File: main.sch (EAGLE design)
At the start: 117 parts, among them Q1 2N2222, Q2 2N2222, Q3 2N2222, Q4 N_MOSFET_DEVSOT23-6L_PKG, U1 MAX_485_DEV3D, U2 BQ24072TRGTR_DEVBQ24072TRGTR, U3 LD1117S33CTR_DEVLD1117S33CTR, U4 ESP_32_WROVER_I_PKG, U5 USB_TO_UART_DEV, U6 AP9214L_DEV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

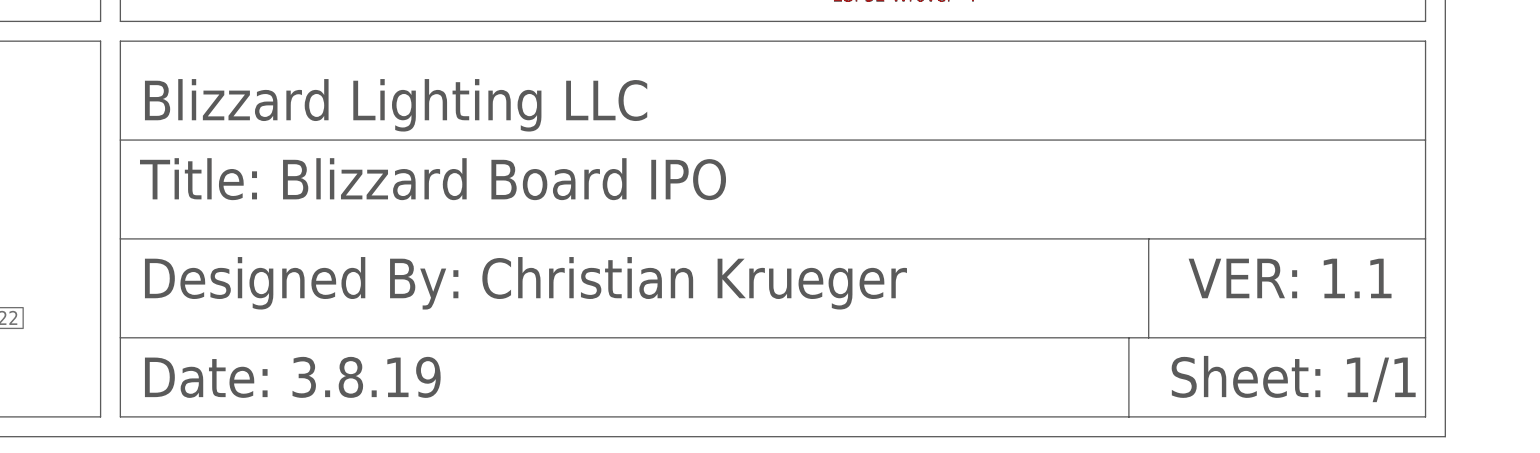
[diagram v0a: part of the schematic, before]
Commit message: fixed tab problems plus made some simplifications
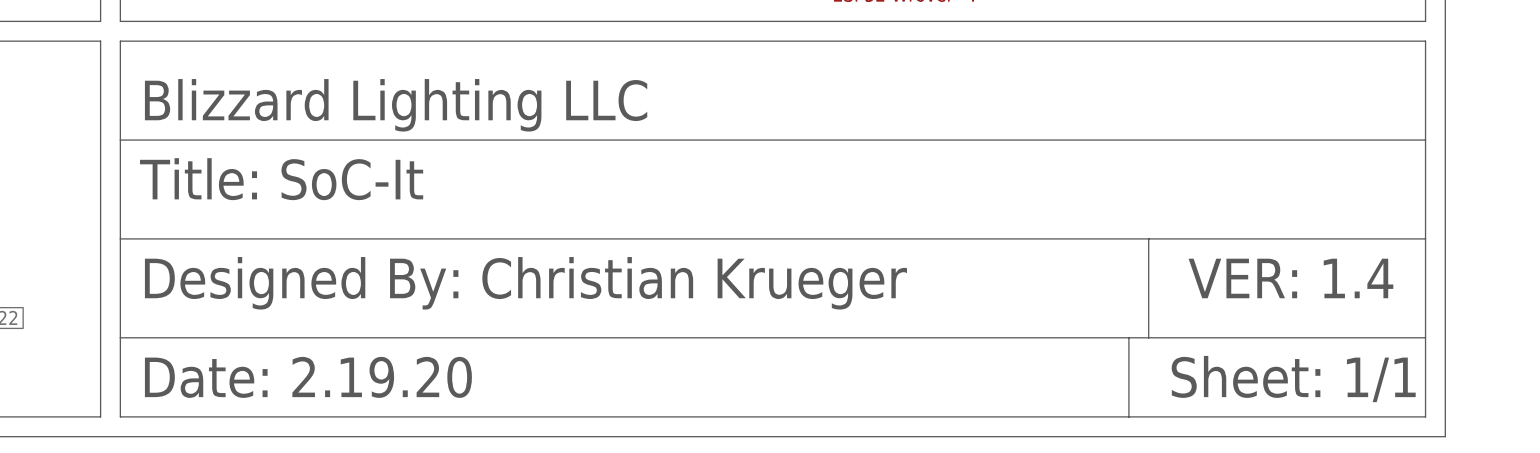
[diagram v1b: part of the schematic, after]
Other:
- note added: "Date: 2.19.20"
- note added: "Title: SoC-It"
- note added: "VER: 1.4"
- note removed: "Date: 3.8.19"
- note removed: "Title: Blizzard Board IPO"
- note removed: "VER: 1.1"
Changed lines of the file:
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@@
 <parts>
 <part name="U1" library="Blizzard_Library" library_urn="urn:adsk.eagle:library:2665040" deviceset="MAX_485_DEV" device="3D" package3d_urn="urn:adsk.eagle:package:2665057/5"/>
-<part name="X1" library="Blizzard_Library" library_urn="urn:adsk.eagle:library:2665040" deviceset="XLR_FEMALE_PLUG_DEV" device="" package3d_urn="urn:adsk.eagle:package:2725172/9"/>
+<part name="X1" library="Blizzard_Library" library_urn="urn:adsk.eagle:library:2665040" deviceset="XLR_FEMALE_PLUG_DEV" device="" package3d_urn="urn:adsk.eagle:package:2725172/12"/>
 <part name="Q1" library="Blizzard_Library" library_urn="urn:adsk.eagle:library:2665040" deviceset="SOT23_TRANS" device="3D" package3d_urn="urn:adsk.eagle:package:2669417/4" value="2N2222"/>
 <part name="Q2" library="Blizzard_Library" library_urn="urn:adsk.eagle:library:2665040" deviceset="SOT23_TRANS" device="3D" package3d_urn="urn:adsk.eagle:package:2669417/4" value="2N2222"/>
@@
 <wire x1="226.06" y1="-302.26" x2="261.62" y2="-302.26" width="0.1524" layer="97"/>
 <wire x1="93.98" y1="-314.96" x2="223.52" y2="-314.96" width="0.1524" layer="97"/>
-<text x="96.52" y="-297.18" size="5.08" layer="97">Title: Blizzard Board IPO</text>
+<text x="96.52" y="-297.18" size="5.08" layer="97">Title: SoC-It</text>
 <text x="96.52" y="-309.88" size="5.08" layer="97">Designed By: Christian Krueger</text>
 <text x="96.52" y="-287.02" size="5.08" layer="97">Blizzard Lighting LLC</text>
-<text x="96.52" y="-322.58" size="5.08" layer="97">Date: 3.8.19</text>
+<text x="96.52" y="-322.58" size="5.08" layer="97">Date: 2.19.20</text>
 <text x="228.6" y="-322.58" size="5.08" layer="97">Sheet: 1/1</text>
-<text x="231.14" y="-309.88" size="5.08" layer="97">VER: 1.1</text>
+<text x="231.14" y="-309.88" size="5.08" layer="97">VER: 1.4</text>
 <wire x1="223.52" y1="-314.96" x2="226.06" y2="-314.96" width="0.1524" layer="97"/>
 <wire x1="226.06" y1="-314.96" x2="261.62" y2="-314.96" width="0.1524" layer="97"/>

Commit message: made the aperature size a bit bigger .3 -> .34
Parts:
- removed VCC: VDD USB, Blizzard_Library:VCC
- added NC30, NC31, NC32, NC33, NC34, NC35, NC36, NC37, NC38, NC39, NC40: NC, Blizzard_Library:NC
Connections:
- new net N$41: NC30.P$1, U5.NC0
- new net N$42: NC31.P$1, U5.NC2
- new net N$43: NC32.P$1, U5.NC1
- new net N$44: NC33.P$1, U5.NC3
- new net N$45: NC34.P$1, U5.NC4
- new net N$46: NC35.P$1, U5.NC5
- new net N$47: NC36.P$1, U5.NC6
- new net N$48: NC37.P$1, U5.NC7
- new net N$49: NC38.P$1, U5.NC8
- new net N$50: NC39.P$1, U5.NC9
- new net N$51: NC40.P$1, U5.NC10
- net VDD_USB: no longer U5.NC0, U5.NC1, U5.NC10, U5.NC2, U5.NC3, U5.NC4, U5.NC5, U5.NC6, U5.NC7, U5.NC8, U5.NC9, VCC.P$1

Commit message: v1.5
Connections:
- net 4.2V: no longer U2.OUT2
- net VBAT: no longer U2.BAT2
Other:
- note added: "VER: 1.5"
- note removed: "VER: 1.4"
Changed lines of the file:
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@@
 <part name="C9" library="Blizzard_Library" library_urn="urn:adsk.eagle:library:2665040" deviceset="0603_CAP_DEV" device="3D" package3d_urn="urn:adsk.eagle:package:2669409/4" value="0.1uF"/>
 <part name="U4" library="Blizzard_Library" library_urn="urn:adsk.eagle:library:2665040" deviceset="ESP_32_WROVER_I_PKG" device="" package3d_urn="urn:adsk.eagle:package:4432905/9"/>
-<part name="U5" library="Blizzard_Library" library_urn="urn:adsk.eagle:library:2665040" deviceset="USB_TO_UART_DEV" device="" package3d_urn="urn:adsk.eagle:package:2665053/7"/>
+<part name="U5" library="Blizzard_Library" library_urn="urn:adsk.eagle:library:2665040" deviceset="USB_TO_UART_DEV" device="" package3d_urn="urn:adsk.eagle:package:2665053/9"/>
 <part name="C11" library="Blizzard_Library" library_urn="urn:adsk.eagle:library:2665040" deviceset="0603_CAP_DEV" device="3D" package3d_urn="urn:adsk.eagle:package:2669409/4" value="0.1uF"/>
 <part name="R16" library="Blizzard_Library" library_urn="urn:adsk.eagle:library:2665040" deviceset="0603_RES_DEV" device="3D" package3d_urn="urn:adsk.eagle:package:2685918/4" value="9K"/>
@@
 <part name="GND19" library="Blizzard_Library" library_urn="urn:adsk.eagle:library:2665040" deviceset="GND" device=""/>
 <part name="C14" library="Blizzard_Library" library_urn="urn:adsk.eagle:library:2665040" deviceset="0603_CAP_DEV" device="3D" package3d_urn="urn:adsk.eagle:package:2669409/4" value="0.1uF"/>
-<part name="U2" library="Blizzard_Library" library_urn="urn:adsk.eagle:library:2665040" deviceset="BQ24072TRGTR_DEV" device="BQ24072TRGTR" package3d_urn="urn:adsk.eagle:package:7249956/7"/>
 <part name="GND8" library="Blizzard_Library" library_urn="urn:adsk.eagle:library:2665040" deviceset="GND" device=""/>
 <part name="GND9" library="Blizzard_Library" library_urn="urn:adsk.eagle:library:2665040" deviceset="GND" device=""/>
@@
 <part name="NC39" library="Blizzard_Library" library_urn="urn:adsk.eagle:library:2665040" deviceset="NC" device=""/>
 <part name="NC40" library="Blizzard_Library" library_urn="urn:adsk.eagle:library:2665040" deviceset="NC" device=""/>
+<part name="U2" library="Blizzard_Library" library_urn="urn:adsk.eagle:library:2665040" deviceset="BQ24072TRGTR_DEV" device="BQ24072TRGTR" package3d_urn="urn:adsk.eagle:package:7249956/11"/>
 </parts>
 <sheets>
@@
 <text x="96.52" y="-322.58" size="5.08" layer="97">Date: 2.19.20</text>
 <text x="228.6" y="-322.58" size="5.08" layer="97">Sheet: 1/1</text>
-<text x="231.14" y="-309.88" size="5.08" layer="97">VER: 1.4</text>
+<text x="231.14" y="-309.88" size="5.08" layer="97">VER: 1.5</text>
 <wire x1="223.52" y1="-314.96" x2="226.06" y2="-314.96" width="0.1524" layer="97"/>
 <wire x1="226.06" y1="-314.96" x2="261.62" y2="-314.96" width="0.1524" layer="97"/>
@@
 <attribute name="VALUE" x="21.336" y="-306.07" size="0.8128" layer="94" rot="R90"/>
 </instance>
-<instance part="U2" gate="G$1" x="93.98" y="-119.38" smashed="yes">
-<attribute name="NAME" x="83.82" y="-104.14" size="1.778" layer="94"/>
-</instance>
 <instance part="GND8" gate="G$1" x="93.98" y="-139.7" smashed="yes"/>
 <instance part="GND9" gate="G$1" x="99.06" y="-139.7" smashed="yes"/>
@@
 <instance part="NC39" gate="G$1" x="251.46" y="-73.66" smashed="yes" rot="R270"/>
 <instance part="NC40" gate="G$1" x="238.76" y="-60.96" smashed="yes"/>
+<instance part="U2" gate="G$1" x="93.98" y="-119.38" smashed="yes">
+<attribute name="NAME" x="76.2" y="-104.14" size="1.778" layer="94"/>
+<attribute name="PN" x="104.14" y="-132.08" size="1.27" layer="94"/>
+</instance>
 </instances>
 <busses>
@@
 </segment>
 <segment>
-<pinref part="U2" gate="G$1" pin="EN1"/>
 <pinref part="GND8" gate="G$1" pin="P$1"/>
 <wire x1="93.98" y1="-137.16" x2="93.98" y2="-134.62" width="0.1524" layer="91"/>
+<pinref part="U2" gate="G$1" pin="EN1"/>
 </segment>
 <segment>
-<pinref part="U2" gate="G$1" pin="VSS"/>
 <wire x1="99.06" y1="-134.62" x2="99.06" y2="-137.16" width="0.1524" layer="91"/>
 <pinref part="GND9" gate="G$1" pin="P$1"/>
+<pinref part="U2" gate="G$1" pin="VSS"/>
 </segment>
 <segment>
 <pinref part="C3" gate="G$1" pin="P$1"/>
-<pinref part="U2" gate="G$1" pin="!CE"/>
 <wire x1="71.12" y1="-121.92" x2="78.74" y2="-121.92" width="0.1524" layer="91"/>
 <wire x1="71.12" y1="-121.92" x2="71.12" y2="-124.46" width="0.1524" layer="91"/>
 <junction x="71.12" y="-121.92"/>
 <pinref part="GND5" gate="G$1" pin="P$1"/>
+<pinref part="U2" gate="G$1" pin="!CE"/>
 </segment>
 <segment>
-<pinref part="U2" gate="G$1" pin="TD/OFF"/>
 <wire x1="93.98" y1="-101.6" x2="93.98" y2="-88.9" width="0.1524" layer="91"/>
 <wire x1="93.98" y1="-88.9" x2="96.52" y2="-88.9" width="0.1524" layer="91"/>
@@
 <wire x1="99.06" y1="-88.9" x2="99.06" y2="-93.98" width="0.1524" layer="91"/>
 <pinref part="C4" gate="G$1" pin="P$2"/>
+<pinref part="U2" gate="G$1" pin="TD/OFF"/>
 </segment>
 <segment>
@@
 </segment>
 <segment>
-<pinref part="U2" gate="G$1" pin="BAT2"/>
-<wire x1="78.74" y1="-119.38" x2="76.2" y2="-119.38" width="0.1524" layer="91"/>
-<wire x1="76.2" y1="-119.38" x2="76.2" y2="-116.84" width="0.1524" layer="91"/>
-<pinref part="U2" gate="G$1" pin="BAT1"/>
-<wire x1="76.2" y1="-116.84" x2="78.74" y2="-116.84" width="0.1524" layer="91"/>
 <pinref part="C3" gate="G$1" pin="P$2"/>
-<wire x1="71.12" y1="-116.84" x2="76.2" y2="-116.84" width="0.1524" layer="91"/>
-<junction x="76.2" y="-116.84"/>
+<wire x1="71.12" y1="-116.84" x2="78.74" y2="-116.84" width="0.1524" layer="91"/>
 <wire x1="71.12" y1="-116.84" x2="71.12" y2="-114.3" width="0.1524" layer="91"/>
 <junction x="71.12" y="-116.84"/>
 <pinref part="VCC6" gate="G$1" pin="P$1"/>
+<pinref part="U2" gate="G$1" pin="BAT1"/>
 </segment>
 <segment>
@@
 </segment>
 <segment>
-<pinref part="U2" gate="G$1" pin="IN"/>
 <wire x1="99.06" y1="-101.6" x2="99.06" y2="-99.06" width="0.1524" layer="91"/>
 <pinref part="C4" gate="G$1" pin="P$1"/>
@@
 <junction x="99.06" y="-99.06"/>
 <pinref part="VCC4" gate="G$1" pin="P$1"/>
+<pinref part="U2" gate="G$1" pin="IN"/>
 </segment>
 <segment>
@@
 </segment>
 <segment>
-<pinref part="U2" gate="G$1" pin="!PGOOD"/>
 <wire x1="96.52" y1="-134.62" x2="96.52" y2="-142.24" width="0.1524" layer="91"/>
 <wire x1="96.52" y1="-142.24" x2="124.46" y2="-142.24" width="0.1524" layer="91"/>
@@
 <pinref part="R12" gate="G$1" pin="P$1"/>
 <wire x1="124.46" y1="-134.62" x2="124.46" y2="-142.24" width="0.1524" layer="91"/>
+<pinref part="U2" gate="G$1" pin="!PGOOD"/>
 </segment>
 </net>
@@
 </segment>
 <segment>
-<pinref part="U2" gate="G$1" pin="!CHG"/>
 <wire x1="111.76" y1="-121.92" x2="111.76" y2="-139.7" width="0.1524" layer="91"/>
 <wire x1="111.76" y1="-139.7" x2="116.84" y2="-139.7" width="0.1524" layer="91"/>
@@
 <pinref part="R11" gate="G$1" pin="P$1"/>
 <wire x1="116.84" y1="-134.62" x2="116.84" y2="-139.7" width="0.1524" layer="91"/>
+<pinref part="U2" gate="G$1" pin="!CHG"/>
 </segment>
 </net>
@@
 </segment>
 <segment>
-<pinref part="U2" gate="G$1" pin="EN2"/>
 <wire x1="91.44" y1="-134.62" x2="91.44" y2="-137.16" width="0.1524" layer="91"/>
 <wire x1="91.44" y1="-137.16" x2="86.36" y2="-137.16" width="0.1524" layer="91"/>
 <wire x1="86.36" y1="-137.16" x2="86.36" y2="-134.62" width="0.1524" layer="91"/>
 <pinref part="VCC8" gate="G$1" pin="P$1"/>
+<pinref part="U2" gate="G$1" pin="EN2"/>
 </segment>
 <segment>
@@
 <pinref part="R11" gate="G$1" pin="P$2"/>
 <wire x1="116.84" y1="-129.54" x2="116.84" y2="-127" width="0.1524" layer="91"/>
-<pinref part="U2" gate="G$1" pin="OUT1"/>
 <wire x1="116.84" y1="-127" x2="116.84" y2="-119.38" width="0.1524" layer="91"/>
 <wire x1="111.76" y1="-119.38" x2="116.84" y2="-119.38" width="0.1524" layer="91"/>
-<wire x1="116.84" y1="-119.38" x2="116.84" y2="-116.84" width="0.1524" layer="91"/>
-<pinref part="U2" gate="G$1" pin="OUT2"/>
-<wire x1="116.84" y1="-116.84" x2="111.76" y2="-116.84" width="0.1524" layer="91"/>
 <junction x="116.84" y="-119.38"/>
 <wire x1="116.84" y1="-127" x2="124.46" y2="-127" width="0.1524" layer="91"/>
@@
 <pinref part="C16" gate="G$1" pin="P$2"/>
 <junction x="129.54" y="-119.38"/>
+<pinref part="U2" gate="G$1" pin="OUT1"/>
 </segment>
 </net>
@@
 <net name="TS" class="0">
 <segment>
-<pinref part="U2" gate="G$1" pin="TS"/>
 <wire x1="78.74" y1="-114.3" x2="76.2" y2="-114.3" width="0.1524" layer="91"/>
 <label x="76.2" y="-114.3" size="1.016" layer="95" rot="R180" xref="yes"/>
+<pinref part="U2" gate="G$1" pin="TS"/>
 </segment>
 <segment>
@@
 <net name="N$35" class="0">
 <segment>
-<pinref part="U2" gate="G$1" pin="TMR"/>
 <wire x1="96.52" y1="-101.6" x2="96.52" y2="-99.06" width="0.1524" layer="91"/>
 <pinref part="R5" gate="G$1" pin="P$1"/>
+<pinref part="U2" gate="G$1" pin="TMR"/>
 </segment>
 </net>
 <net name="N$37" class="0">
 <segment>
-<pinref part="U2" gate="G$1" pin="ISET"/>
 <wire x1="91.44" y1="-101.6" x2="91.44" y2="-99.06" width="0.1524" layer="91"/>
 <pinref part="R4" gate="G$1" pin="P$1"/>
+<pinref part="U2" gate="G$1" pin="ISET"/>
 </segment>
 </net>
 <net name="N$34" class="0">
 <segment>
-<pinref part="U2" gate="G$1" pin="ILIM"/>
 <wire x1="111.76" y1="-114.3" x2="116.84" y2="-114.3" width="0.1524" layer="91"/>
 <wire x1="116.84" y1="-114.3" x2="116.84" y2="-111.76" width="0.1524" layer="91"/>
 <pinref part="R6" gate="G$1" pin="P$1"/>
+<pinref part="U2" gate="G$1" pin="ILIM"/>
 </segment>
 </net>
